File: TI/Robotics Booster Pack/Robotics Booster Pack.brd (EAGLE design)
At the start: 68.6 x 76.2 mm, 111 parts, among them J1 1X2.PTS, U1 TS3A44159.RGT, U10 74LVTH125.RGY, U11 SCHA4B0400, U12 BLUETOOTH-RN41", U13 XBEE-1XBEE-1_LOCK, U14 TPS54X0, U2 TPS62082.DSG, U3 DRV8800, U4 DRV8800, U5 DRV8800, U6 DRV8800, U7 PCA9557.RGV, U8 MPU-6050, U9 INA220.DGS

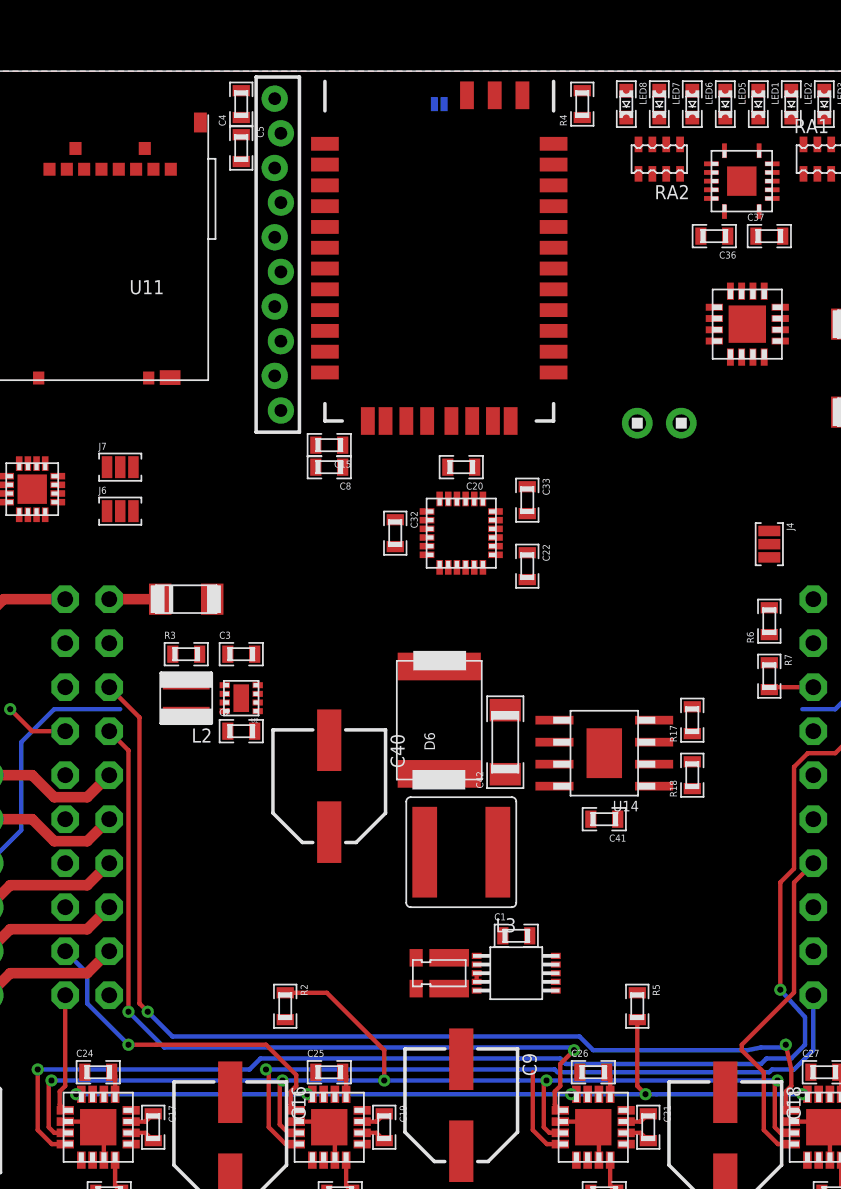
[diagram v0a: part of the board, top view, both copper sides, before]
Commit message: Modifed Robotics BP regulators, along with a few other things
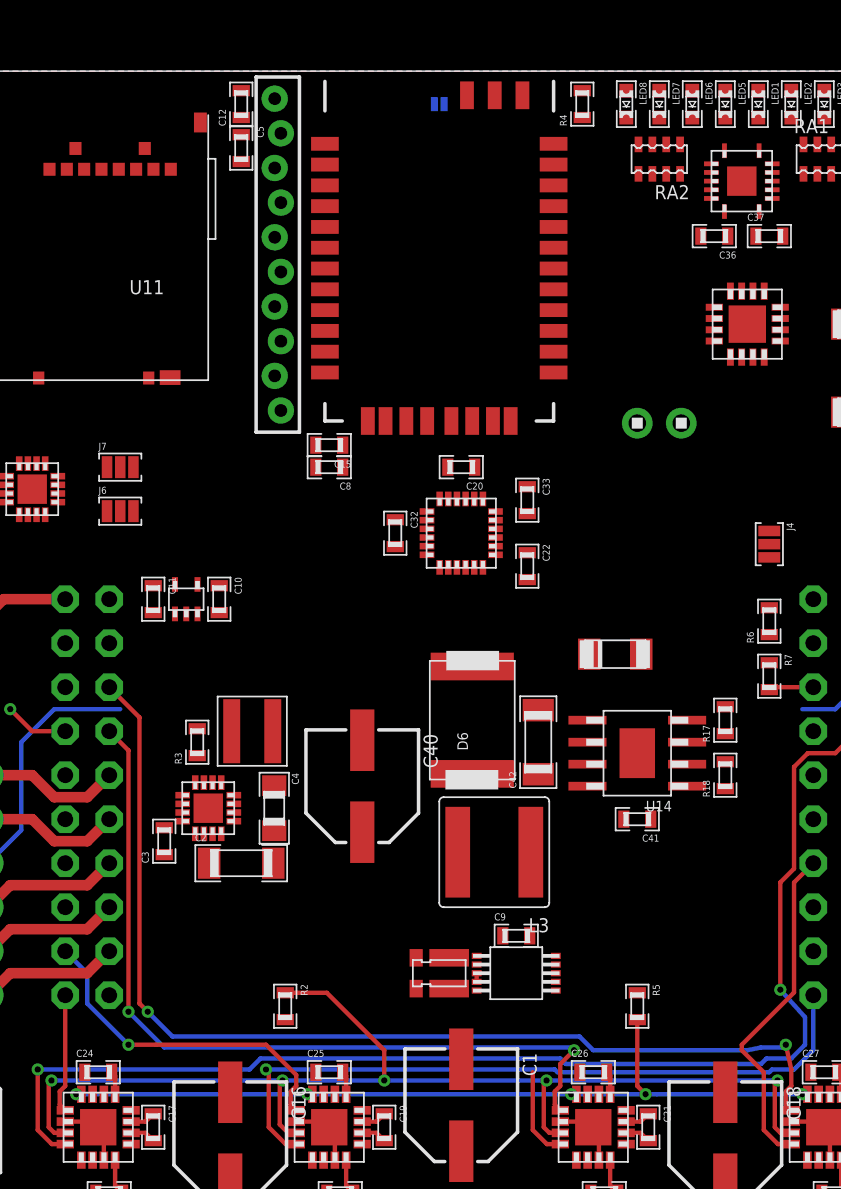
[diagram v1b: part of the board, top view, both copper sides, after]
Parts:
- removed L2: 1uH, bourns:SRN3015
- removed U2: TPS62082.DSG, packages(ti):DSG
- added C10, C12: .1uF, standardparts:0603
- added C11: 1uF, standardparts:0603
- added L1: 2.2uH, coilcraft:XAL4020
- added U15: TPS715XX.DCK, packages(ti):DCK
- added U16: TPS6215X.RGT, packages(ti):RGT.16
- C1: value .1uF -> 100uF; device standardparts:0603 -> microbuilder:PANASONIC_D
- C2: device standardparts:0603 -> standardparts:1206
- C3: value 22uF -> 330nF
- C4: value .1uF -> 22uF; device standardparts:0603 -> standardparts:0805
- C9: value 100uF -> .1uF; device microbuilder:PANASONIC_D -> standardparts:0603
- L3: value INDUCTOR.XAL6060 -> (none)
- R3: value 178k -> 100k
- U14: value TPS54X0 -> TPS5450
- moved C4 40.7 mm to (23.5, 33.7), turned to 270 degrees
- moved D2 25.0 mm to (43.2, 42.5)
- moved C3 11.7 mm to (17.1, 31.8), turned to 90 degrees
- moved C1 10.3 mm to (34.3, 16.5), turned to 270 degrees
- moved C9 10.3 mm to (37.5, 26.3), turned to 0 degrees
- moved C2 7.62 mm to (21.6, 30.5)
- moved R3 5.12 mm to (19.1, 37.5), turned to 90 degrees
- moved C41 1.91 mm to (44.5, 33.0)
- moved C42 1.91 mm to (38.7, 37.5)
- moved L3 1.91 mm to (36.2, 31.1)
- moved R17 1.91 mm to (49.5, 38.7)
- moved R18 1.91 mm to (49.5, 35.6)
- moved U14 1.91 mm to (44.5, 36.8)
- moved C40 1.90 mm to (28.6, 34.9)
- moved D6 1.90 mm to (34.9, 38.7)
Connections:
- removed net N$12: L2.1, U2.7
- new net N$23: C3.1, U16.9
- new net VBUS: C11.1, U$8.VBUS, U15.5
- net 3.3V: now also C12.1, C9.1, L1.2, U16.14, U16.7; no longer C1.1, C3.1, L2.2, U2.5
- net 3.3V.PG: now also U16.4; no longer U2.6
- net 5.0V: no longer C2.1, D2.2, U2.8
- net 5V.PG: no longer U2.1
- net GND: now also C10.2, C11.2, C12.2, C9.2, U15.2, U16.15, U16.16, U16.5, U16.6, U16.8, U16.PAD; no longer C1.2, U2.2, U2.3, U2.PAD
- net N$1: now also L1.1, U16.1, U16.2, U16.3; no longer D2.1, U$8.VBUS
- net N$22: now also C1.+; no longer C9.+
- net VBAT: now also C10.1, C2.1, U15.4, U16.10, U16.11, U16.12, U16.13
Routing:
- net N$1: track 2.94 -> 0.00 mm

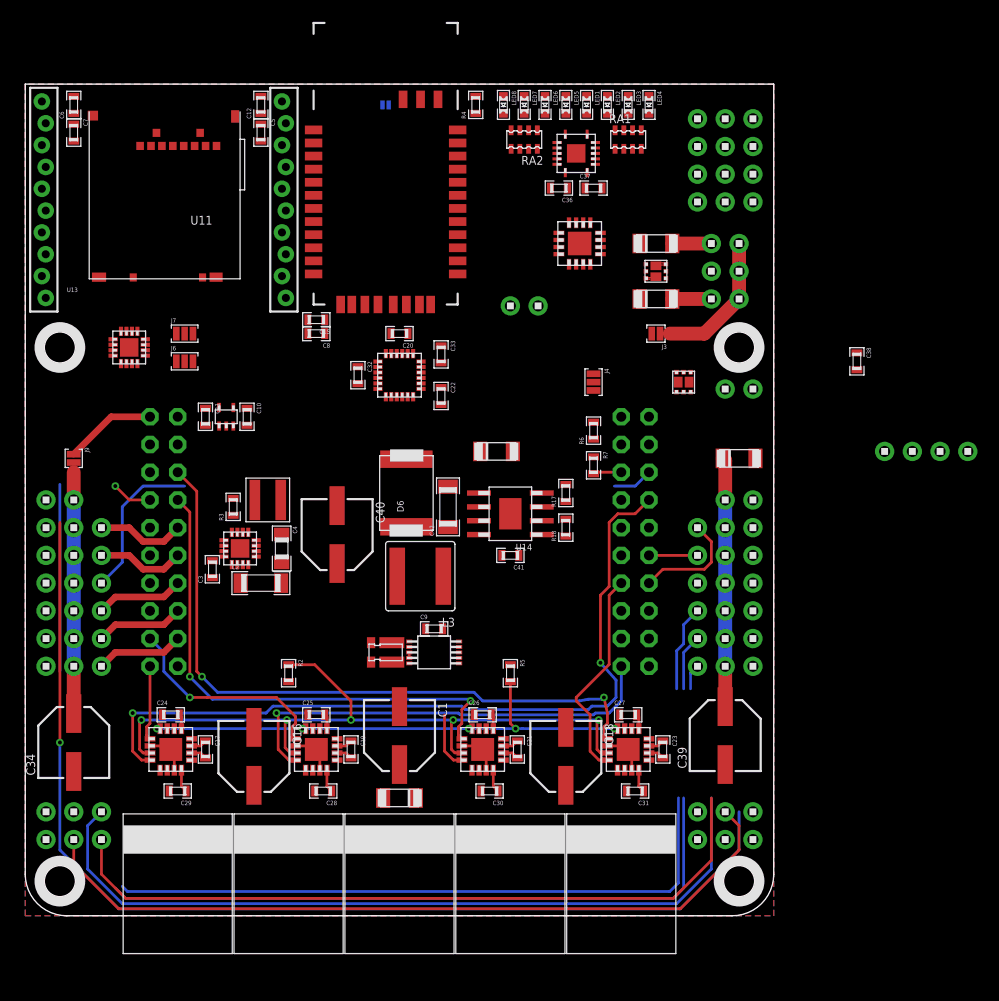
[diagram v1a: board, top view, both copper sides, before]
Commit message: Cleaned up Servo.EN connections and indicator LEDs Routing will soon begin. It's unreasonable to believe that it will all be complete by the end of the weekend, bu some goals aren't meant to be met.
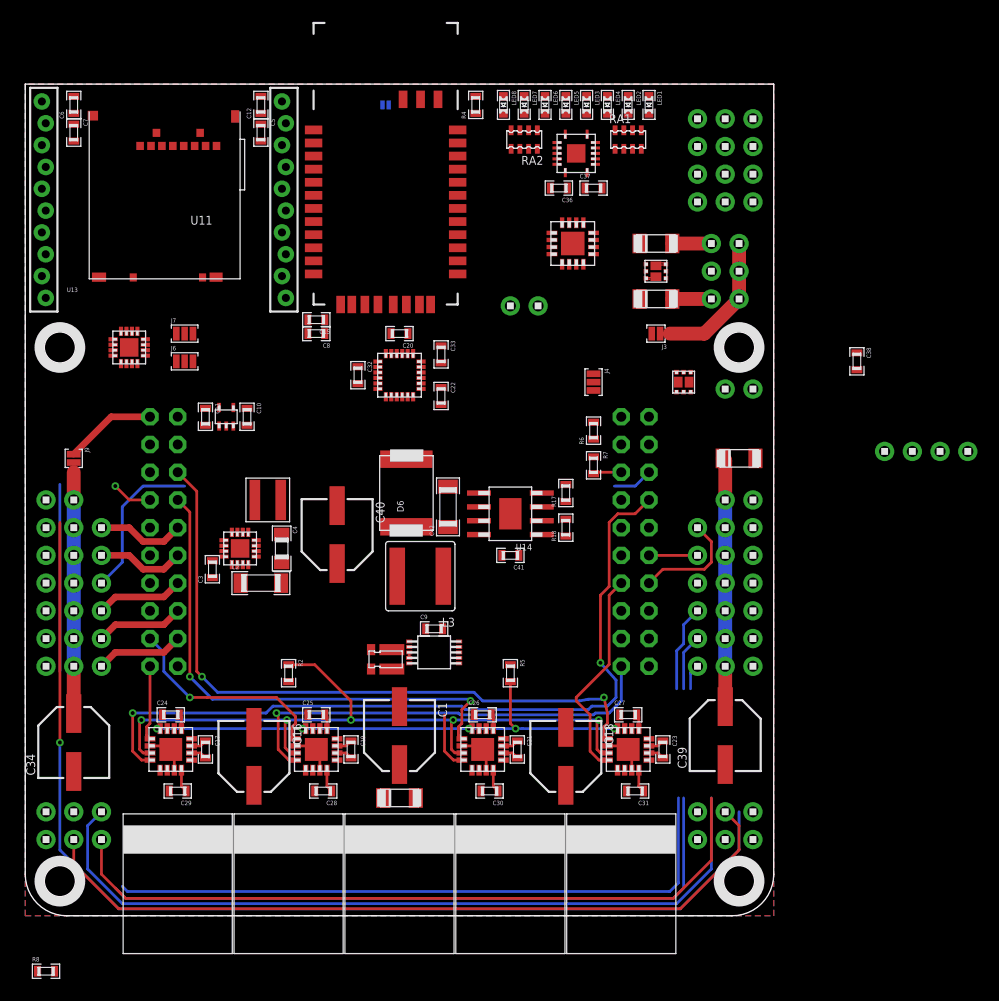
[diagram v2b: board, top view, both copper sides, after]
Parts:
- removed D2: CDBMT2100-HF, comchip:SOD-123H
- removed R3: 100k, standardparts:0603
- added R8: 10k, standardparts:0603
- moved LED1 5.71 mm to (57.1, 74.3)
- moved LED3 3.81 mm to (51.4, 74.3)
- moved LED4 3.81 mm to (53.3, 74.3)
- moved LED2 1.90 mm to (55.2, 74.3)
- moved R1 0.63 mm to (33.0, 23.5)
- moved U7 0.63 mm to (50.2, 61.6), turned to 0 degrees
- turned D1 to 0 degrees
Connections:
- removed net 3.3V.PG: R3.1, U10.12, U16.4
- removed net 5V.PG: U10.9
- removed net N$28: LED1.P$2, U10.3
- new net N$12: LED4.P$2, RA1.4
- new net SVRO.EN: Q2.2, Q2.5, R8.1
- net 3.3V: now also U10.2; no longer R3.2
- net 5.0V: now also U10.5
- net GND: now also R8.2
- net IO0: now also U7.12; no longer U7.10
- net IO1: now also U7.11; no longer U7.9
- net IO2: now also U7.10; no longer U7.8
- net IO3: now also U7.9; no longer U7.7
- net M.EN: now also U10.12, U7.8; no longer U7.11
- net N$10: now also U10.6; no longer RA1.4
- net N$11: now also U10.3; no longer RA1.2
- net N$26: now also LED3.P$2, RA1.2; no longer LED2.P$2, U10.6
- net N$5: now also LED1.P$2; no longer LED4.P$2
- net N$8: now also LED2.P$2; no longer LED3.P$2
- net SRVO.EN: now also U10.9, U7.7; no longer Q2.2, Q2.5, U7.12
- net UART0.RXI: now also U$15.2
- net UART0.TXO: now also U$15.1
- net UART1.RXI: no longer U10.5
- net UART1.TXO: no longer U10.2
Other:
- board text added: "Motors ON"
- board text added: "Servos ON"
- board text removed: "RxI"
- board text removed: "TxO"

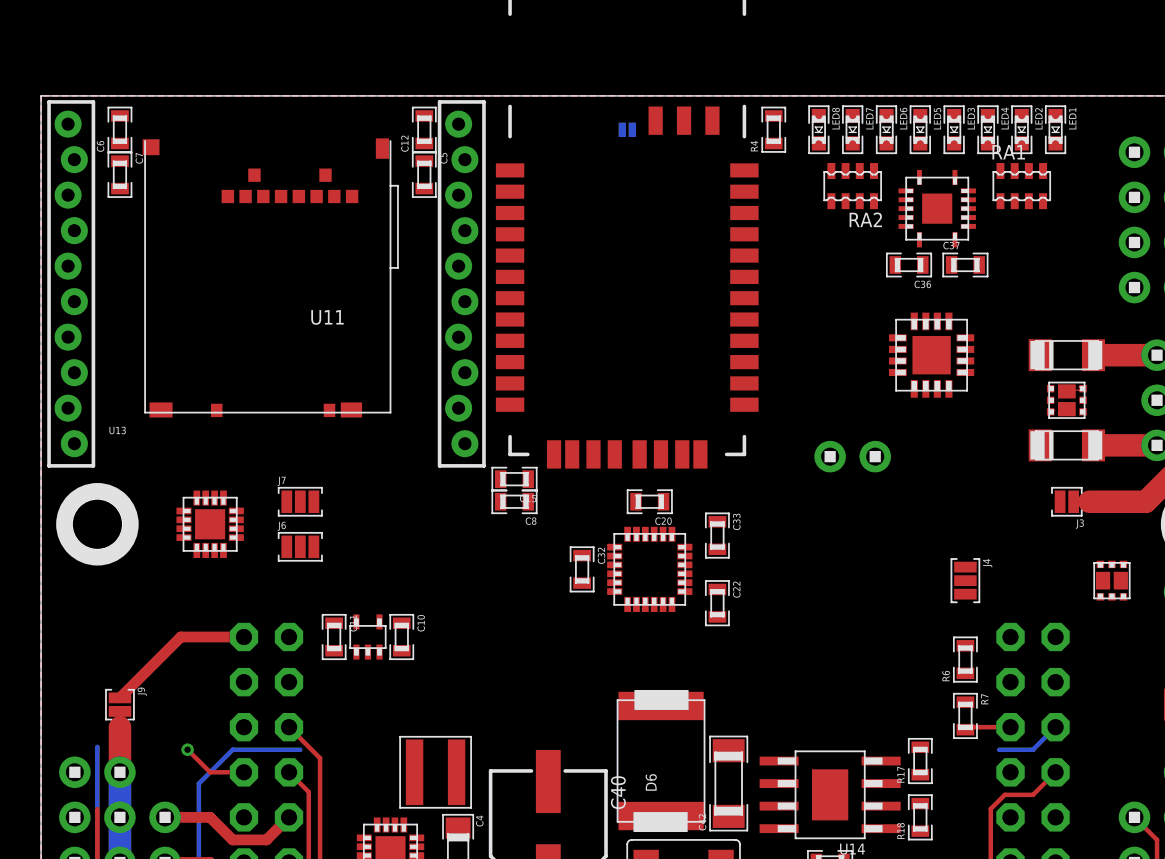
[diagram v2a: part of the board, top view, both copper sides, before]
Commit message: Began routing of Robotics BP v2 Bluetooth, XBee, and UART mux routing nearly complete. Started LEDs and IMU routing.
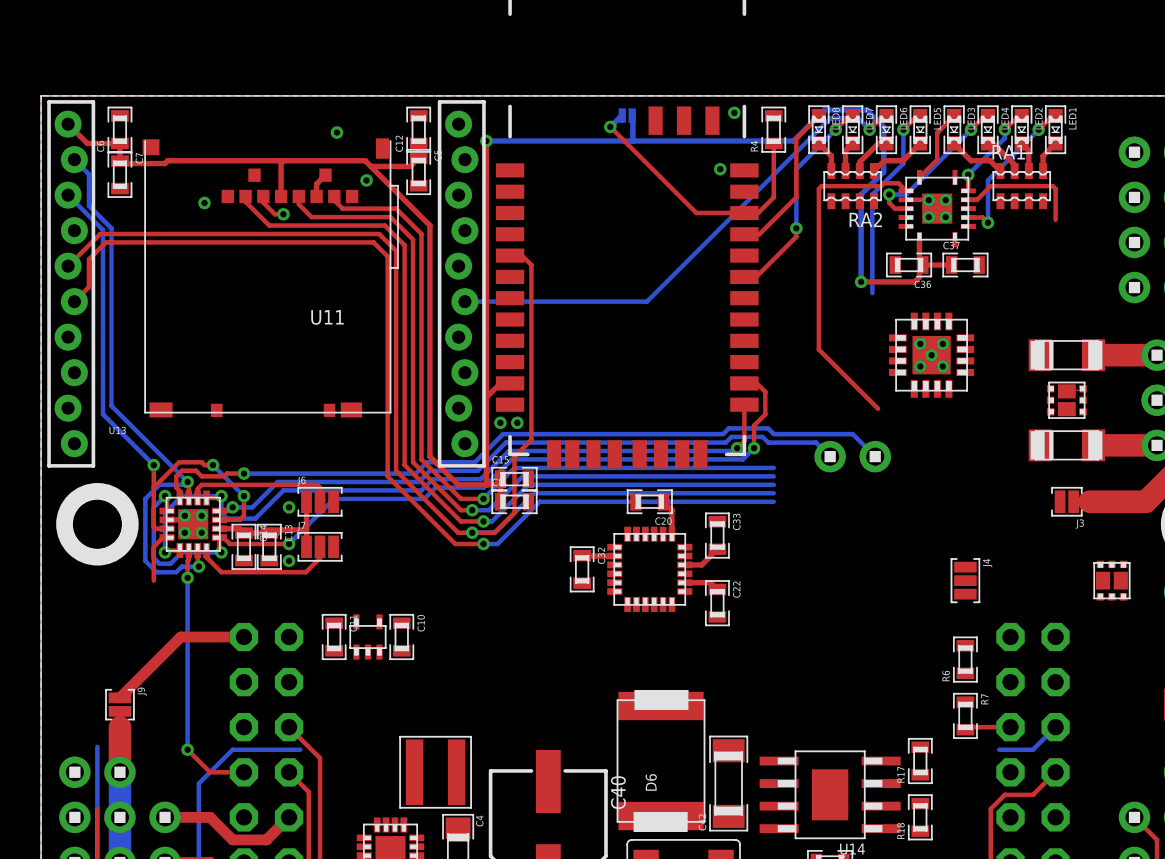
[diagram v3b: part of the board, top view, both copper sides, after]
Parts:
- added C13: .1uF, standardparts:0603
- added C14: 1uF, standardparts:0603
- moved J6 2.77 mm to (15.7, 53.3)
- moved J7 2.77 mm to (15.7, 50.8)
- moved U1 0.95 mm to (8.57, 52.1), turned to 270 degrees
- moved J2 0.79 mm to (33.0, 75.1), turned to 180 degrees
- moved C5 0.35 mm to (21.3, 71.9)
- moved C12 0.32 mm to (21.3, 74.3)
- turned C15 to 0 degrees
- turned C8 to 0 degrees
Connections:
- net 3.3V: now also C13.1, C14.1
- net GND: now also C13.2, C14.2
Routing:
- net 3.3V: track 79.6 -> 202.2 mm, vias 0 -> 2
- net !RST: track 0.00 -> 74.3 mm, vias 0 -> 1
- net XBEE.RSSI: track 0.00 -> 68.2 mm, vias 0 -> 2
- net BT.RXI: track 0.00 -> 47.0 mm, vias 0 -> 4
- net SPI.!CS: track 0.00 -> 45.6 mm, vias 0 -> 1
- net UART0.RXI: track 0.00 -> 42.7 mm, vias 0 -> 1
- net SPI.SCLK: track 0.00 -> 42.5 mm, vias 0 -> 1
- net BT.TXO: track 0.00 -> 42.0 mm, vias 0 -> 3
- net SPI.MISO: track 0.00 -> 40.1 mm, vias 0 -> 1
- net UART0.TXO: track 0.00 -> 36.6 mm, vias 0 -> 1
- net XBEE.RXI: track 0.00 -> 32.3 mm, vias 0 -> 2
- net XBEE.TXO: track 0.00 -> 30.5 mm, vias 0 -> 3
- net XBEE.ASSOCIATE: track 0.00 -> 28.6 mm, vias 0 -> 1
- net SRVO.EN: track 0.00 -> 19.0 mm
- net BT.RESET: track 0.00 -> 15.6 mm, vias 0 -> 1
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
